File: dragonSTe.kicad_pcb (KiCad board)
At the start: 2 copper layers, 255 parts, among them J2 MIDI OUT, J3 MIDI IN, J4 DB25_Socket, J5 DB25_Pins, J6 Keyboard, J7 Internal FDD, SW1 RESET, U1 68000, U30 LF347DT, U32 LF347DT, U33 LM78L82, U34 LMC1992, U37 DMA, U38 WD1772, U39 STB, U40 GST_SHIFTER, U5 LM555xM, U7 MC6850, U8 MC6850, U9 YM2149, X1 8.010613MHz

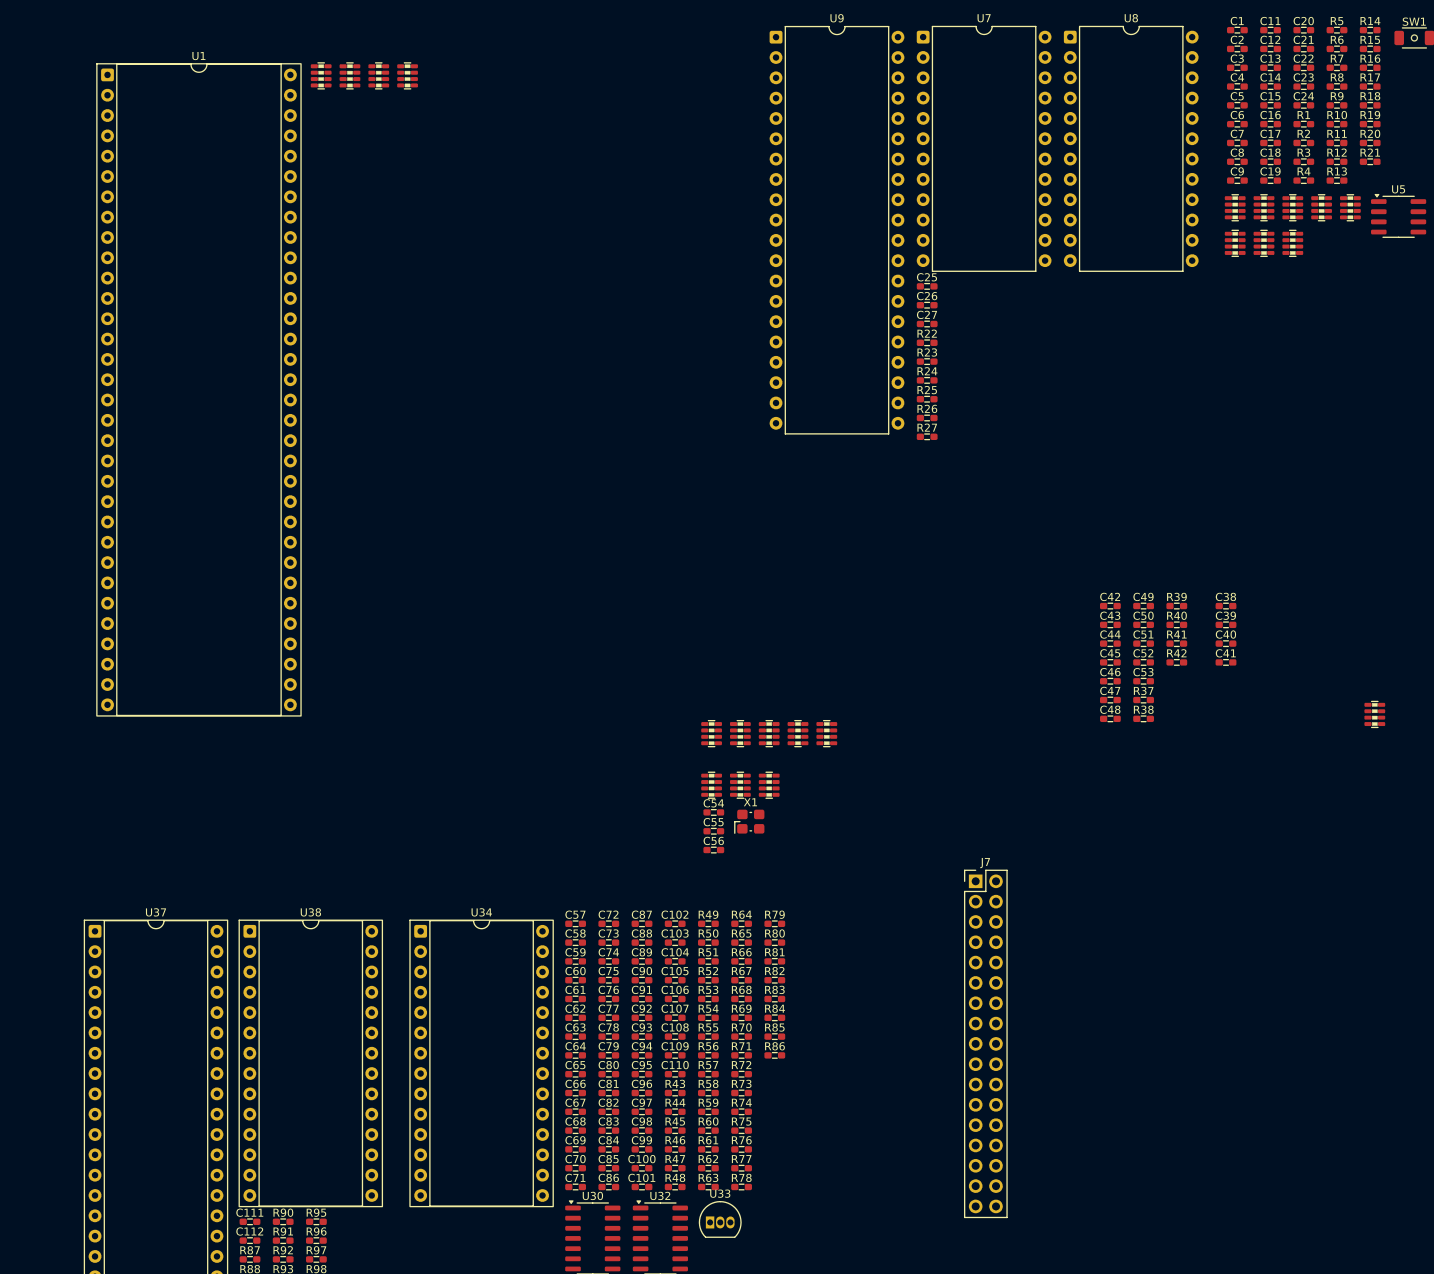
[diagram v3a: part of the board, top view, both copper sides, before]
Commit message: motherboard: Worked on fleshing out more of the top-level schematic, filling in more of the connections that need to be made between blocks
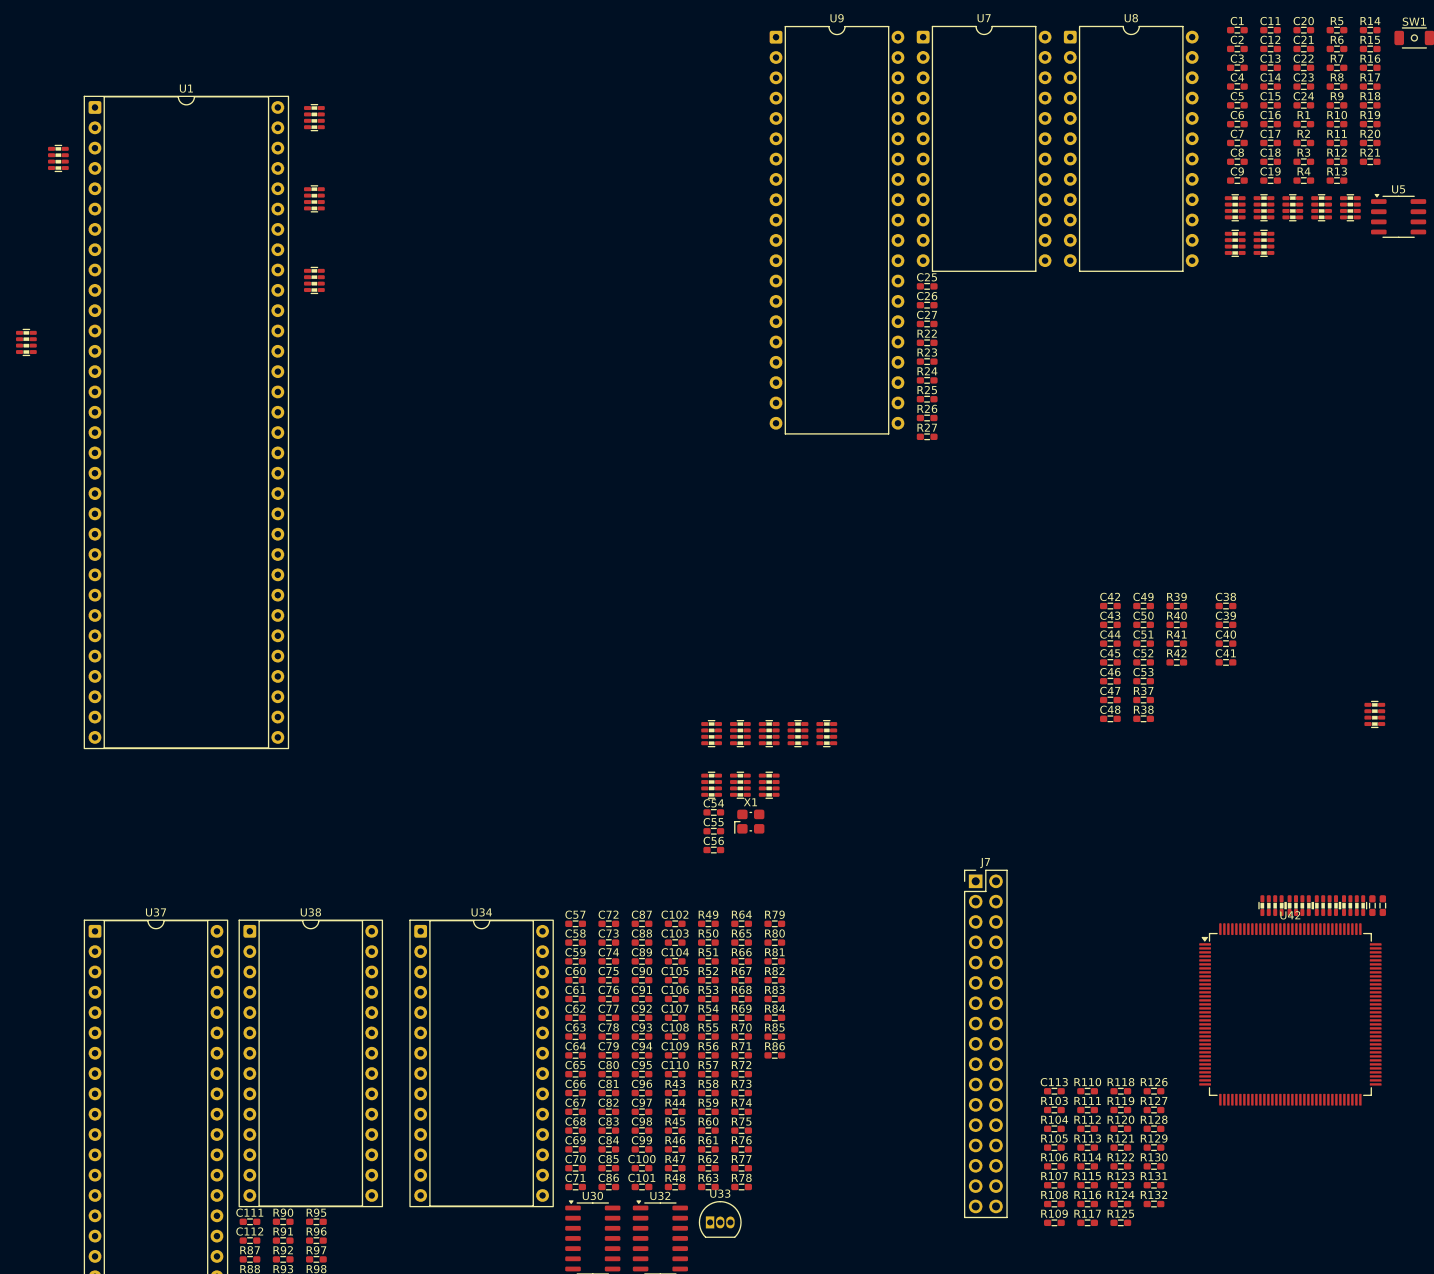
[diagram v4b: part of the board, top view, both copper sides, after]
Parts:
- added C113: 100n, rhais_rcl:C0603, F.Cu at (208.5, 183.6)
- added R103: 12k, rhais_rcl:R0603, F.Cu at (208.5, 185.9)
- added R104: 1k5, rhais_rcl:R0603, F.Cu at (208.5, 188.3)
- added R105: 3k, rhais_rcl:R0603, F.Cu at (208.5, 190.7)
- added R106: 6k2, rhais_rcl:R0603, F.Cu at (208.5, 193.0)
- added R107: 12k, rhais_rcl:R0603, F.Cu at (208.5, 195.3)
- added R108: 1k5, rhais_rcl:R0603, F.Cu at (208.5, 197.7)
- added R109: 3k, rhais_rcl:R0603, F.Cu at (208.5, 200.1)
- added R110: 6k2, rhais_rcl:R0603, F.Cu at (212.7, 183.6)
- added R111: 12k, rhais_rcl:R0603, F.Cu at (212.7, 185.9)
- added R112: 1k5, rhais_rcl:R0603, F.Cu at (212.7, 188.3)
- added R113: 3k, rhais_rcl:R0603, F.Cu at (212.7, 190.7)
- added R114: 6k2, rhais_rcl:R0603, F.Cu at (212.7, 193.0)
- added R115: 1k, rhais_rcl:R0603, F.Cu at (212.7, 195.3)
- added R116: 2k, rhais_rcl:R0603, F.Cu at (212.7, 197.7)
- added R117: 1k, rhais_rcl:R0603, F.Cu at (212.7, 200.1)
- added R118: 2k, rhais_rcl:R0603, F.Cu at (216.8, 183.6)
- added R119: 1k, rhais_rcl:R0603, F.Cu at (216.8, 185.9)
- added R120: 2k, rhais_rcl:R0603, F.Cu at (216.8, 188.3)
- added R121: 75R, rhais_rcl:R0603, F.Cu at (216.8, 190.7)
- added R122: 75R, rhais_rcl:R0603, F.Cu at (216.8, 193.0)
- added R123: 75R, rhais_rcl:R0603, F.Cu at (216.8, 195.3)
- added R124: 75R, rhais_rcl:R0603, F.Cu at (216.8, 197.7)
- added R125: 75R, rhais_rcl:R0603, F.Cu at (216.8, 200.1)
- added R126: 75R, rhais_rcl:R0603, F.Cu at (220.9, 183.6)
- added R127: 75R, rhais_rcl:R0603, F.Cu at (220.9, 185.9)
- added R128: 75R, rhais_rcl:R0603, F.Cu at (220.9, 188.3)
- added R129: 75R, rhais_rcl:R0603, F.Cu at (220.9, 190.7)
- added R130: 1k, rhais_rcl:R0603, F.Cu at (220.9, 193.0)
- added R131: 100R, rhais_rcl:R0603, F.Cu at (220.9, 195.3)
- added R132: 27R, rhais_rcl:R0603, F.Cu at (220.9, 197.7)
- added R133: 68R, rhais_rcl:R0603, F.Cu at (248.2, 160.4)
- added R134: 68R, rhais_rcl:R0603, F.Cu at (249.6, 160.4)
- added RN22: 68R, rhais_rcl:R0603_Array_Concave_4, F.Cu at (242.5, 160.4)
- added RN23: 68R, rhais_rcl:R0603_Array_Concave_4, F.Cu at (245.9, 160.4)
- added RN24: 33R, rhais_rcl:R0603_Array_Concave_4, F.Cu at (239.1, 160.4)
- added RN25: 33R, rhais_rcl:R0603_Array_Concave_4, F.Cu at (235.7, 160.4)
- added U42: GST_MCU, Package_QFP:LQFP-144_20x20mm_P0.5mm, F.Cu at (238.0, 174.0)
- moved RN12 158.8 mm to (80.0, 90.0)
- moved RN4 44.8 mm to (84.0, 67.0)
- moved RN1 25.6 mm to (116.0, 82.2)
- moved RN2 16.0 mm to (116.0, 72.0)
- moved RN3 9.59 mm to (116.0, 61.9)
- moved U1 4.36 mm to (88.6, 60.6)
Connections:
- R102 pad 2: unconnected-(R102-Pad2) -> Net-(Q9-PadB)
- U1 pad 23: unconnected-(U1-IPL2-Pad23) -> /CPU+ROMs/~{IPL2}
- U1 pad 24: unconnected-(U1-IPL1-Pad24) -> /CPU+ROMs/~{IPL1}
- U1 pad 25: unconnected-(U1-IPL0-Pad25) -> /CPU+ROMs/~{IPL0}
- U37 pad 1: /Disk & Floppy/SysBus.R/~{W} -> /CPU+ROMs/SysBus.R/~{W}
- U37 pad 12: /Disk & Floppy/SysBus.D8 -> /CPU+ROMs/SysBus.D8
- U37 pad 13: /Disk & Floppy/SysBus.D9 -> /CPU+ROMs/SysBus.D9
- U37 pad 14: /Disk & Floppy/SysBus.D10 -> /CPU+ROMs/SysBus.D10
- U37 pad 15: /Disk & Floppy/SysBus.D11 -> /CPU+ROMs/SysBus.D11
- U37 pad 16: /Disk & Floppy/SysBus.D12 -> /CPU+ROMs/SysBus.D12
- U37 pad 17: /Disk & Floppy/SysBus.D13 -> /CPU+ROMs/SysBus.D13
- U37 pad 18: /Disk & Floppy/SysBus.D14 -> /CPU+ROMs/SysBus.D14
- U37 pad 19: /Disk & Floppy/SysBus.D15 -> /CPU+ROMs/SysBus.D15
- U37 pad 2: /Disk & Floppy/SysBus.A1 -> /CPU+ROMs/SysBus.A1
- U40 pad 1: /Video/SysBus.D7 -> /CPU+ROMs/SysBus.D7
- U40 pad 10: /Video/SysBus.R/~{W} -> /CPU+ROMs/SysBus.R/~{W}
- U40 pad 12: /Video/SysBus.A6 -> /CPU+ROMs/SysBus.A6
- U40 pad 13: /Video/SysBus.A5 -> /CPU+ROMs/SysBus.A5
- U40 pad 14: /Video/SysBus.A4 -> /CPU+ROMs/SysBus.A4
- U40 pad 15: /Video/SysBus.A3 -> /CPU+ROMs/SysBus.A3
- U40 pad 16: /Video/SysBus.A2 -> /CPU+ROMs/SysBus.A2
- U40 pad 17: /Video/SysBus.A1 -> /CPU+ROMs/SysBus.A1
- U40 pad 18: unconnected-(U40-~{CS}-Pad18) -> Net-(U40-~{CS})
- U40 pad 2: /Video/SysBus.D8 -> /CPU+ROMs/SysBus.D8
- U40 pad 3: /Video/SysBus.D9 -> /CPU+ROMs/SysBus.D9
- U40 pad 35: unconnected-(U40-~{SLOAD}-Pad35) -> Net-(U40-~{SLOAD})
- U40 pad 36: unconnected-(U40-SREQ-Pad36) -> Net-(U40-SREQ)
- U40 pad 37: unconnected-(U40-~{LOAD}-Pad37) -> Net-(U40-~{LOAD})
- U40 pad 38: unconnected-(U40-R3-Pad38) -> Net-(U40-R3)
- U40 pad 39: unconnected-(U40-R2-Pad39) -> Net-(U40-R2)
- U40 pad 4: /Video/SysBus.D10 -> /CPU+ROMs/SysBus.D10
- U40 pad 40: unconnected-(U40-R1-Pad40) -> Net-(U40-R1)
- U40 pad 41: unconnected-(U40-R0-Pad41) -> Net-(U40-R0)
- U40 pad 42: unconnected-(U40-G3-Pad42) -> Net-(U40-G3)
- U40 pad 43: unconnected-(U40-G2-Pad43) -> Net-(U40-G2)
- U40 pad 44: unconnected-(U40-G1-Pad44) -> Net-(U40-G1)
- U40 pad 45: unconnected-(U40-G0-Pad45) -> Net-(U40-G0)
- U40 pad 46: unconnected-(U40-B3-Pad46) -> Net-(U40-B3)
- U40 pad 47: unconnected-(U40-B2-Pad47) -> Net-(U40-B2)
- U40 pad 48: unconnected-(U40-B1-Pad48) -> Net-(U40-B1)
- U40 pad 49: unconnected-(U40-B0-Pad49) -> Net-(U40-B0)
- U40 pad 5: /Video/SysBus.D11 -> /CPU+ROMs/SysBus.D11
- U40 pad 52: unconnected-(U40-CLK16MHz-Pad52) -> Net-(U40-CLK16MHz)
- U40 pad 55: unconnected-(U40-~{BLANK}-Pad55) -> Net-(U40-~{BLANK})
- U40 pad 56: unconnected-(U40-MD0-Pad56) -> /Video/RAM.D0
- U40 pad 57: unconnected-(U40-MD1-Pad57) -> /Video/RAM.D1
- U40 pad 58: unconnected-(U40-MD2-Pad58) -> /Video/RAM.D2
- U40 pad 59: unconnected-(U40-MD3-Pad59) -> /Video/RAM.D3
- U40 pad 6: /Video/SysBus.D12 -> /CPU+ROMs/SysBus.D12
- U40 pad 60: unconnected-(U40-MD4-Pad60) -> /Video/RAM.D4
- U40 pad 61: unconnected-(U40-MD5-Pad61) -> /Video/RAM.D5
- U40 pad 62: unconnected-(U40-MD6-Pad62) -> /Video/RAM.D6
- U40 pad 63: unconnected-(U40-MD7-Pad63) -> /Video/RAM.D7
- U40 pad 64: unconnected-(U40-MD8-Pad64) -> /Video/RAM.D8
- U40 pad 65: unconnected-(U40-MD9-Pad65) -> /Video/RAM.D9
- U40 pad 66: unconnected-(U40-MD10-Pad66) -> /Video/RAM.D10
- U40 pad 67: unconnected-(U40-MD11-Pad67) -> /Video/RAM.D11
- U40 pad 68: unconnected-(U40-MD12-Pad68) -> /Video/RAM.D12
- U40 pad 69: unconnected-(U40-MD13-Pad69) -> /Video/RAM.D13
- U40 pad 7: /Video/SysBus.D13 -> /CPU+ROMs/SysBus.D13
- U40 pad 70: unconnected-(U40-MD14-Pad70) -> /Video/RAM.D14
- U40 pad 71: unconnected-(U40-MD15-Pad71) -> /Video/RAM.D15
- U40 pad 72: unconnected-(U40-~{WDATA}-Pad72) -> Net-(U40-~{WDATA})
- U40 pad 76: unconnected-(U40-LATCH-Pad76) -> Net-(U40-LATCH)
- U40 pad 77: unconnected-(U40-~{RDATA}-Pad77) -> Net-(U40-~{RDATA})
- U40 pad 78: /Video/SysBus.D0 -> /CPU+ROMs/SysBus.D0
- U40 pad 79: /Video/SysBus.D1 -> /CPU+ROMs/SysBus.D1
- U40 pad 8: /Video/SysBus.D14 -> /CPU+ROMs/SysBus.D14
- U40 pad 80: /Video/SysBus.D2 -> /CPU+ROMs/SysBus.D2
- U40 pad 81: /Video/SysBus.D3 -> /CPU+ROMs/SysBus.D3
- U40 pad 82: /Video/SysBus.D4 -> /CPU+ROMs/SysBus.D4
- U40 pad 83: /Video/SysBus.D5 -> /CPU+ROMs/SysBus.D5
- U40 pad 84: /Video/SysBus.D6 -> /CPU+ROMs/SysBus.D6
- U40 pad 9: /Video/SysBus.D15 -> /CPU+ROMs/SysBus.D15
- U7 pad 11: /IO Interfaces/SysBus.A1 -> /CPU+ROMs/SysBus.A1
- U7 pad 13: /IO Interfaces/SysBus.R/~{W} -> /CPU+ROMs/SysBus.R/~{W}
- U7 pad 14: /IO Interfaces/SysBus.E -> /CPU+ROMs/SysBus.E
- U7 pad 15: /IO Interfaces/SysBus.D15 -> /CPU+ROMs/SysBus.D15
- U7 pad 16: /IO Interfaces/SysBus.D14 -> /CPU+ROMs/SysBus.D14
- U7 pad 17: /IO Interfaces/SysBus.D13 -> /CPU+ROMs/SysBus.D13
- U7 pad 18: /IO Interfaces/SysBus.D12 -> /CPU+ROMs/SysBus.D12
- U7 pad 19: /IO Interfaces/SysBus.D11 -> /CPU+ROMs/SysBus.D11
- U7 pad 20: /IO Interfaces/SysBus.D10 -> /CPU+ROMs/SysBus.D10
- U7 pad 21: /IO Interfaces/SysBus.D9 -> /CPU+ROMs/SysBus.D9
- U7 pad 22: /IO Interfaces/SysBus.D8 -> /CPU+ROMs/SysBus.D8
- U7 pad 9: /IO Interfaces/SysBus.A2 -> /CPU+ROMs/SysBus.A2
- U8 pad 10: /IO Interfaces/SysBus.A2 -> /CPU+ROMs/SysBus.A2
- U8 pad 11: /IO Interfaces/SysBus.A1 -> /CPU+ROMs/SysBus.A1
- U8 pad 13: /IO Interfaces/SysBus.R/~{W} -> /CPU+ROMs/SysBus.R/~{W}
- U8 pad 14: /IO Interfaces/SysBus.E -> /CPU+ROMs/SysBus.E
- U8 pad 15: /IO Interfaces/SysBus.D15 -> /CPU+ROMs/SysBus.D15
- U8 pad 16: /IO Interfaces/SysBus.D14 -> /CPU+ROMs/SysBus.D14
- U8 pad 17: /IO Interfaces/SysBus.D13 -> /CPU+ROMs/SysBus.D13
- U8 pad 18: /IO Interfaces/SysBus.D12 -> /CPU+ROMs/SysBus.D12
- U8 pad 19: /IO Interfaces/SysBus.D11 -> /CPU+ROMs/SysBus.D11
- U8 pad 20: /IO Interfaces/SysBus.D10 -> /CPU+ROMs/SysBus.D10
- U8 pad 21: /IO Interfaces/SysBus.D9 -> /CPU+ROMs/SysBus.D9
- U8 pad 22: /IO Interfaces/SysBus.D8 -> /CPU+ROMs/SysBus.D8
- U9 pad 30: /IO Interfaces/SysBus.D15 -> /CPU+ROMs/SysBus.D15
- U9 pad 31: /IO Interfaces/SysBus.D14 -> /CPU+ROMs/SysBus.D14
- U9 pad 32: /IO Interfaces/SysBus.D13 -> /CPU+ROMs/SysBus.D13
- U9 pad 33: /IO Interfaces/SysBus.D12 -> /CPU+ROMs/SysBus.D12
- U9 pad 34: /IO Interfaces/SysBus.D11 -> /CPU+ROMs/SysBus.D11
- U9 pad 35: /IO Interfaces/SysBus.D10 -> /CPU+ROMs/SysBus.D10
- U9 pad 36: /IO Interfaces/SysBus.D9 -> /CPU+ROMs/SysBus.D9
- U9 pad 37: /IO Interfaces/SysBus.D8 -> /CPU+ROMs/SysBus.D8
